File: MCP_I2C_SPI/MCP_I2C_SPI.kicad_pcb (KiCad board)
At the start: 2 copper layers, 136 x 95 mm, 46 parts, among them J1 GPA, J10 VCC, J11 GND, J12 I2C, J13 Interrupt0, J14 A2, J15 A1, J16 A0, J17 SDA, J18 SCK, J19 INTA, J2 GPB, J20 INTB, J21 V0, J22 Ext, J23 SPI, J24 InterruptS, J25 A2, J27 GPB, J28 GPA, J29 A1, J3 Data, J31 A0, J32 INTA, J33 INTB, J4 Control, J5 Zlacze_LCD, J6 VSS, J7 K, J8 VDD, J9 A, U1 MCP23017_SP, U2 MCP23017_SP

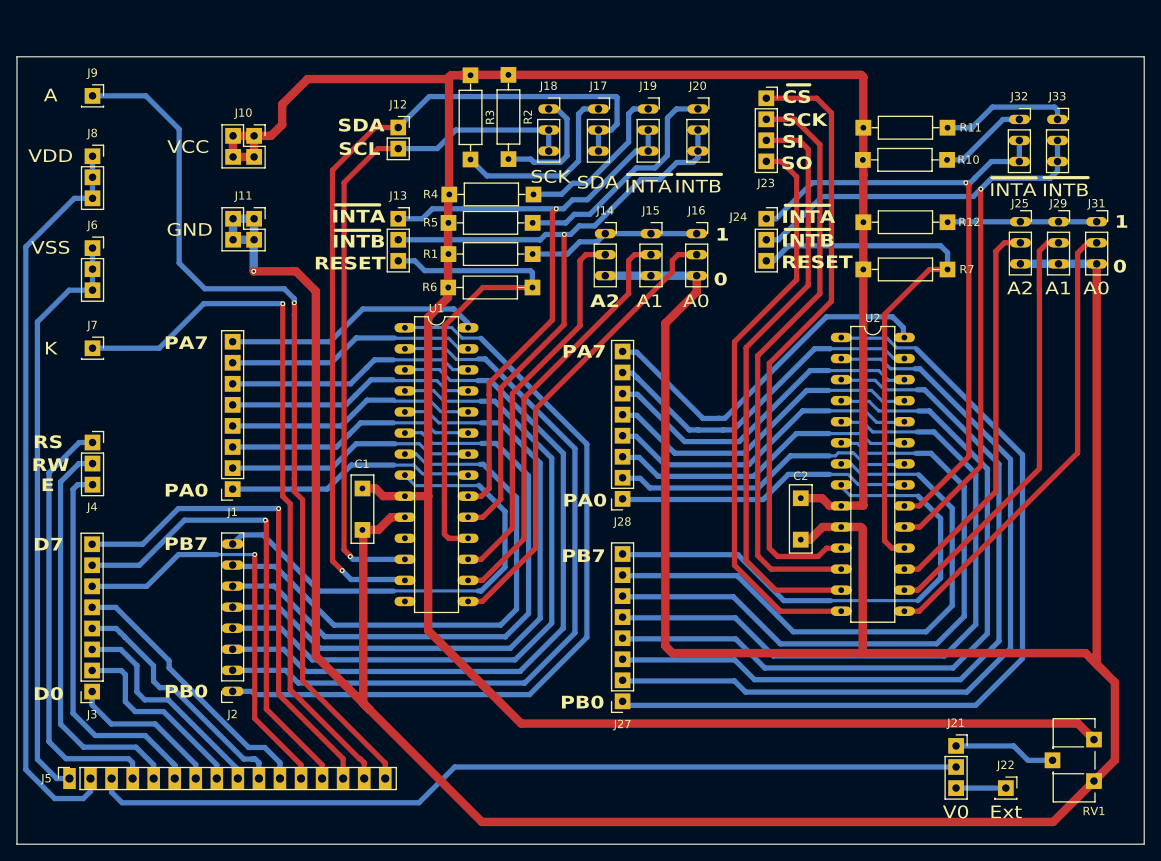
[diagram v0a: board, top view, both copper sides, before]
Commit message: Zmiana footprintu rezystorow - 6mm
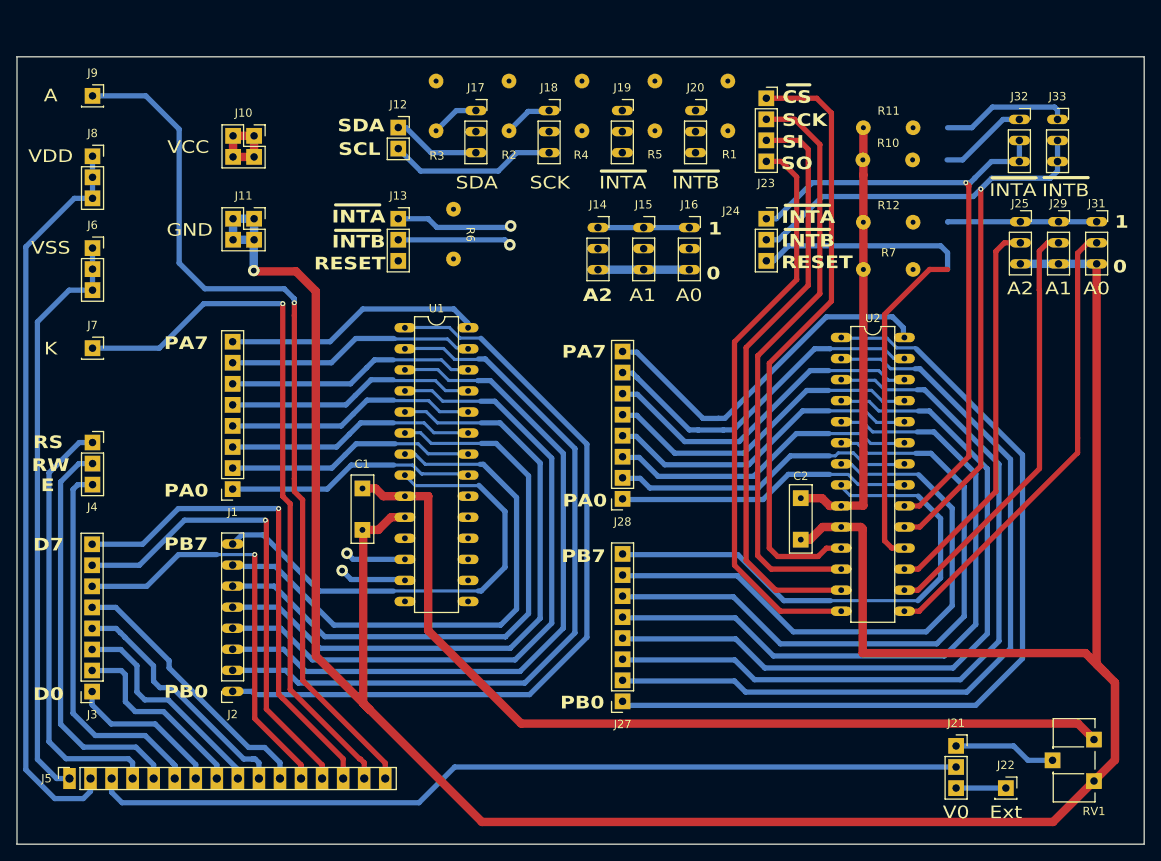
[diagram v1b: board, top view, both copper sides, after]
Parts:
- R1, R10, R11, R12, R2, R3, R4, R5, R6, R7: footprint Library:R_Axial_DIN0207_L6.3mm_D2.5mm_P10.16mm_Horizontal_square -> Library:Resistor_6mm
- moved R1 39.6 mm to (137.7, 28.2), turned to -90 degrees
- moved R5 30.2 mm to (128.9, 28.2), turned to -90 degrees
- moved R4 21.1 mm to (120.1, 28.2), turned to -90 degrees
- moved J17 14.8 mm to (107.3, 31.8)
- moved R6 9.47 mm to (104.6, 43.7), turned to -90 degrees
- moved R3 4.21 mm to (102.5, 28.2)
- moved J19 3.13 mm to (125.0, 31.8)
- moved J14 1.14 mm to (122.0, 45.9)
- moved J15 1.14 mm to (127.5, 45.9)
- moved J16 1.14 mm to (133.1, 45.9)
- moved R2 0.75 mm to (111.3, 28.2)
- moved J20 0.35 mm to (133.8, 31.8)
- moved J18 0.20 mm to (116.1, 31.8)
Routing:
- net +5V: track 311.0 -> 174.0 mm
- net SDA: track 103.2 -> 18.7 mm
- net GND: track 408.4 -> 338.0 mm
- net INTB0: track 83.6 -> 13.9 mm
- net INTA0: track 76.1 -> 14.2 mm
- net RESET0: track 60.0 -> 0.00 mm
- net Net-(J16-Pin_2): track 55.6 -> 0.00 mm
- net SCL: track 82.4 -> 27.5 mm
- net Net-(J15-Pin_2): track 50.6 -> 0.00 mm
- net Net-(J14-Pin_2): track 45.9 -> 0.00 mm
- net Net-(J20-Pin_1): track 28.3 -> 0.00 mm
- net Net-(J19-Pin_1): track 20.1 -> 0.00 mm
- net Net-(J17-Pin_1): track 22.9 -> 5.81 mm
- net Net-(J14-Pin_1): track 20.8 -> 11.0 mm
- net Net-(J18-Pin_1): track 14.7 -> 5.87 mm

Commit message: Update PCB MCP_I2C_SPI V3
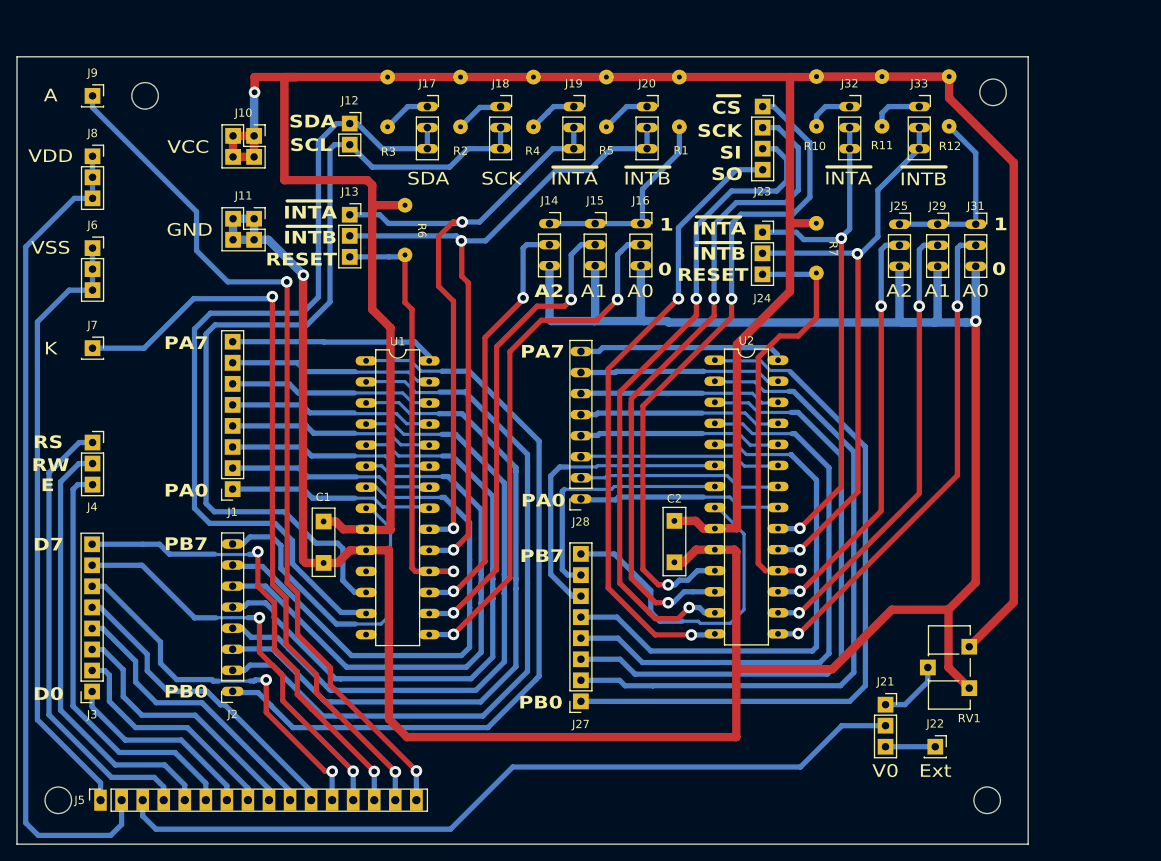
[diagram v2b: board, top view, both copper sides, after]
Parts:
- added REF**: MountingHole_3.2mm_M3, MountingHole:MountingHole_3.2mm_M3, F.Cu at (67.4, 30.0)
- added REF**: MountingHole_3.2mm_M3, MountingHole:MountingHole_3.2mm_M3, F.Cu at (56.9, 115.0)
- added REF**: MountingHole_3.2mm_M3, MountingHole:MountingHole_3.2mm_M3, F.Cu at (169.7, 29.6)
- added REF**: MountingHole_3.2mm_M3, MountingHole:MountingHole_3.2mm_M3, F.Cu at (169.0, 115.0)
- moved J32 20.5 mm to (152.4, 31.3)
- moved R12 20.4 mm to (164.4, 27.7), turned to -90 degrees
- moved RV1 18.8 mm to (166.8, 101.5)
- moved J33 16.7 mm to (160.8, 31.3)
- moved C2 15.5 mm to (131.3, 81.3)
- moved U2 15.5 mm to (136.1, 61.9)
- moved J29 14.6 mm to (163.0, 45.5)
- moved J25 14.6 mm to (158.4, 45.5)
- moved J31 14.6 mm to (167.6, 45.5)
- moved R10 11.5 mm to (148.4, 27.7), turned to -90 degrees
- moved J21 9.87 mm to (156.7, 103.5)
- moved J22 9.87 mm to (162.7, 108.6)
- moved R7 7.95 mm to (148.4, 45.4), turned to -90 degrees
- moved R11 6.57 mm to (156.3, 27.7), turned to -90 degrees
- moved C1 6.16 mm to (88.9, 81.4)
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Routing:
- net +5V: track 174.0 -> 322.8 mm, vias 0 -> 1
- net SDA: track 18.7 -> 102.3 mm, vias 1 -> 0
- net SCL: track 27.5 -> 106.8 mm, vias 1 -> 0
- net INTB0: track 13.9 -> 84.8 mm, vias 1 -> 2
- net Net-(J16-Pin_2): track 0.00 -> 64.2 mm, vias 0 -> 2
- net INTA0: track 14.2 -> 76.3 mm, vias 1 -> 2
- net Net-(J15-Pin_2): track 0.00 -> 57.6 mm, vias 0 -> 2
- net RESET0: track 0.00 -> 53.0 mm, vias 0 -> 1
- net Net-(J14-Pin_2): track 0.00 -> 51.3 mm, vias 0 -> 2
- net Net-(J27-Pin_7): track 71.2 -> 30.6 mm
- net Net-(J27-Pin_6): track 77.6 -> 38.0 mm
- net Net-(J27-Pin_8): track 62.6 -> 39.4 mm
- net Net-(J28-Pin_8): track 43.9 -> 24.9 mm
- net Net-(J27-Pin_5): track 83.8 -> 65.3 mm
- net Net-(J27-Pin_4): track 88.0 -> 70.0 mm
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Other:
- board size 136 x 95 mm -> 122 x 95 mm

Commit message: płytka MCP 17.06.2026
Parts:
- moved RV1 16.7 mm to (161.6, 85.6)
- moved J14 11.7 mm to (104.5, 45.4)
- moved J16 11.7 mm to (115.5, 45.4)
- moved J15 11.7 mm to (110.0, 45.4)
- moved J21 11.7 mm to (145.2, 105.6)
- moved J22 11.0 mm to (151.8, 107.9)
- moved J23 7.38 mm to (141.8, 38.7), turned to 180 degrees
- moved R6 6.65 mm to (92.1, 43.3)
- moved J10 6.58 mm to (74.0, 35.7)
- moved J11 6.58 mm to (74.0, 45.7)
- moved J25 6.23 mm to (152.3, 44.3)
- moved J29 6.23 mm to (156.9, 44.3)
- moved J31 6.23 mm to (161.5, 44.3)
- moved R1 6.10 mm to (125.8, 27.7)
- moved J20 5.88 mm to (122.1, 31.3)
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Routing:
- net INTB0: track 84.8 -> 129.0 mm
- net INTBS: track 71.3 -> 95.4 mm
- net Net-(J21-Pin_1): track 7.97 -> 30.4 mm
- net +5V: track 322.8 -> 304.9 mm
- net INTA0: track 76.3 -> 89.3 mm
- net Net-(J21-Pin_2): track 97.4 -> 85.0 mm
- net CS: track 81.2 -> 69.1 mm
- net GND: track 326.1 -> 337.8 mm
- net SO: track 75.3 -> 86.3 mm
- net Net-(J14-Pin_1): track 24.6 -> 30.4 mm
- net SCK: track 82.4 -> 76.8 mm
- net Net-(J16-Pin_2): track 64.2 -> 59.2 mm
- net Net-(J15-Pin_2): track 57.6 -> 53.2 mm
- net Net-(J5-Pin_15): track 91.2 -> 86.9 mm
- net RESETS: track 54.1 -> 50.4 mm
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
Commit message: kolejna wersja MCP
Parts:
- J10, J11: footprint Library:PinSocket_2x02_P2.54mm_Vertical_kwadrat -> Library:PinSocket_1x03_P2.54mm_Vertical
- moved RV1 32.4 mm to (140.6, 110.3), turned to 90 degrees
- moved R1 30.8 mm to (99.4, 43.6)
- moved J22 18.6 mm to (133.1, 108.1)
- moved J21 16.9 mm to (128.3, 105.5)
- moved J31 10.2 mm to (151.3, 44.3)
- moved J33 10.2 mm to (148.9, 31.2)
- moved R11 10.2 mm to (145.3, 27.7)
- moved J23 10.2 mm to (131.6, 38.7)
- moved J24 10.2 mm to (131.7, 46.5)
- moved J25 10.2 mm to (142.1, 44.3)
- moved J29 10.2 mm to (146.7, 44.3)
- moved J32 10.2 mm to (141.8, 31.3)
- moved R10 10.2 mm to (138.2, 27.7)
- moved R12 10.2 mm to (152.4, 27.7)
- moved R7 8.66 mm to (137.9, 45.3)
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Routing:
- net INTB0: track 129.0 -> 100.6 mm
- net GND: track 337.8 -> 312.7 mm
- net Net-(J27-Pin_8): track 39.4 -> 20.8 mm
- net Net-(J21-Pin_2): track 85.0 -> 68.1 mm
- net Net-(J21-Pin_1): track 30.4 -> 14.9 mm
- net +5V: track 304.9 -> 317.5 mm
- net Net-(J14-Pin_1): track 30.4 -> 19.4 mm
- net INTA0: track 89.3 -> 83.3 mm
- net Net-(J31-Pin_2): track 63.0 -> 57.1 mm
- net INTBS: track 95.4 -> 99.4 mm
- net CS: track 69.1 -> 65.4 mm
- net INTAS: track 63.5 -> 66.7 mm
- net SCL: track 103.6 -> 101.1 mm
- net RESETS: track 50.4 -> 52.9 mm
- net SDA: track 101.6 -> 99.2 mm
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
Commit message: MCP_I2C_SPI_V5
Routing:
- net INTA0: track 83.3 -> 86.3 mm
- net INTB0: track 100.6 -> 103.5 mm
- net SCK: track 74.6 -> 73.1 mm
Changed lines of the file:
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@@
 		)
 		(property "Value" "V0"
-			(at -3.6576 2.3114 0)
+			(at -3.8608 2.6538 0)
 			(layer "F.SilkS")
 			(effects
@@
 		)
 		(property "Value" "Ext"
-			(at -0.1778 3.0734 0)
+			(at -0.1214 3.373 0)
 			(layer "F.SilkS")
 			(effects
@@
 			)
 		)
-		(pad "1" thru_hole oval
+		(pad "1" thru_hole rect
 			(at 0 0)
-			(size 2.54 1.143)
-			(drill 0.508)
+			(size 1.905 1.905)
+			(drill 0.9)
 			(layers "*.Cu" "*.Mask")
 			(remove_unused_layers no)
@@
 			(pintype "passive")
 		)
-		(pad "2" thru_hole oval
+		(pad "2" thru_hole rect
 			(at 0 2.54)
-			(size 2.54 1.143)
-			(drill 0.508)
+			(size 1.905 1.905)
+			(drill 0.9)
 			(layers "*.Cu" "*.Mask")
 			(remove_unused_layers no)
@@
 			(pintype "passive")
 		)
-		(pad "3" thru_hole oval
+		(pad "3" thru_hole rect
 			(at 0 5.08)
-			(size 2.54 1.143)
-			(drill 0.508)
+			(size 1.905 1.905)
+			(drill 0.9)
 			(layers "*.Cu" "*.Mask")
 			(remove_unused_layers no)
@@
 			)
 		)
-		(pad "1" thru_hole oval
+		(pad "1" thru_hole rect
 			(at 0 0)
-			(size 2.54 1.143)
-			(drill 0.508)
+			(size 1.905 1.905)
+			(drill 0.9)
 			(layers "*.Cu" "*.Mask")
 			(remove_unused_layers no)
@@
 			(pintype "passive")
 		)
-		(pad "2" thru_hole oval
+		(pad "2" thru_hole rect
 			(at 0 2.54)
-			(size 2.54 1.143)
-			(drill 0.508)
+			(size 1.905 1.905)
+			(drill 0.9)
 			(layers "*.Cu" "*.Mask")
 			(remove_unused_layers no)
@@
 			(pintype "passive")
 		)
-		(pad "3" thru_hole oval
+		(pad "3" thru_hole rect
 			(at 0 5.08)
-			(size 2.54 1.143)
-			(drill 0.508)
+			(size 1.905 1.905)
+			(drill 0.9)
 			(layers "*.Cu" "*.Mask")
 			(remove_unused_layers no)
@@
 	)
 	(segment
-		(start 88.9289 95.932422)
-		(end 92.8878 99.891322)
+		(start 130.5306 90.5002)
+		(end 130.5306 86.8788)
 		(width 1.016)
 		(layer "F.Cu")
@@
 	)
 	(segment
-		(start 130.5306 90.5002)
-		(end 130.5306 86.8788)
+		(start 83.9617 56.547952)
+		(end 83.9617 80.244266)
 		(width 1.016)
 		(layer "F.Cu")
@@
 	)
 	(segment
-		(start 83.9617 56.547952)
-		(end 83.9617 80.244266)
+		(start 125.349 103.3018)
+		(end 125.349 98.8822)
 		(width 1.016)
 		(layer "F.Cu")
@@
 	)
 	(segment
-		(start 96.7926 105.2)
-		(end 96.8 105.2)
+		(start 80.981348 53.550348)
+		(end 80.981348 53.5676)
 		(width 1.016)
 		(layer "F.Cu")
@@
 	)
 	(segment
-		(start 125.349 103.3018)
-		(end 125.349 98.8822)
+		(start 92.72 99.723522)
+		(end 92.72 101.12)
 		(width 1.016)
 		(layer "F.Cu")
@@
 	)
 	(segment
-		(start 80.981348 53.550348)
-		(end 80.981348 53.5676)
+		(start 92.72 101.12)
+		(end 99 107.4)
 		(width 1.016)
 		(layer "F.Cu")
@@
 	)
 	(segment
-		(start 85.765499 82.048063)
-		(end 85.765501 85.365501)
+		(start 121.2508 107.4)
+		(end 125.349 103.3018)
 		(width 1.016)
 		(layer "F.Cu")
@@
 	)
 	(segment
-		(start 80.981348 53.5676)
-		(end 83.9617 56.547952)
+		(start 85.765499 82.048063)
+		(end 85.765501 85.365501)
 		(width 1.016)
 		(layer "F.Cu")
@@
 	)
 	(segment
-		(start 99 107.4)
-		(end 121.2508 107.4)
+		(start 80.981348 53.5676)
+		(end 83.9617 56.547952)
 		(width 1.016)
 		(layer "F.Cu")
@@
 	)
 	(segment
-		(start 92.8878 101.2952)
-		(end 96.7926 105.2)
+		(start 88.9289 95.932422)
+		(end 92.72 99.723522)
 		(width 1.016)
 		(layer "F.Cu")
@@
 	)
 	(segment
-		(start 96.8 105.2)
-		(end 99 107.4)
+		(start 99 107.4)
+		(end 121.2508 107.4)
 		(width 1.016)
 		(layer "F.Cu")
@@
 	)
 	(segment
-		(start 88.9289 86.385)
-		(end 88.9289 95.932422)
-		(width 1.016)
-		(layer "F.Cu")
-		(net 1)
-	)
-	(segment
 		(start 140.6144 98.8822)
 		(end 125.349 98.8822)
@@
 	)
 	(segment
-		(start 85.765501 85.365501)
-		(end 86.785 86.385)
+		(start 88.9289 86.385)
+		(end 88.9289 95.932422)
 		(width 1.016)
 		(layer "F.Cu")
@@
 	)
 	(segment
-		(start 92.8878 99.891322)
-		(end 92.8878 101.2952)
+		(start 85.765501 85.365501)
+		(end 86.785 86.385)
 		(width 1.016)
 		(layer "F.Cu")
@@
 	)
 	(segment
-		(start 121.2508 107.4)
-		(end 125.349 103.3018)
-		(width 1.016)
-		(layer "F.Cu")
-		(net 1)
-	)
-	(segment
 		(start 125.349 95.6818)
 		(end 130.5306 90.5002)
@@
 	)
 	(segment
-		(start 81.9614 89.175)
-		(end 84.112 91.3256)
-		(width 0.381)
-		(layer "B.Cu")
-		(net 14)
-	)
-	(segment
 		(start 107.938982 90.070622)
 		(end 107.93898 91.228744)
@@
 	)
 	(segment
+		(start 81.9614 89.175)
+		(end 84.112 91.3256)
+		(width 0.381)
+		(layer "B.Cu")
+		(net 14)
+	)
+	(segment
 		(start 95.93178 74.6593)
 		(end 95.1016 74.6593)
@@
 	)
 	(segment
-		(start 84.112 92.85734)
-		(end 90.20866 98.954)
-		(width 0.381)
-		(layer "B.Cu")
-		(net 14)
-	)
-	(segment
 		(start 107.938992 88.912478)
 		(end 107.938988 88.912482)
@@
 	)
 	(segment
-		(start 90.20866 98.954)
-		(end 91.726929 98.954)
+		(start 84.112 92.85734)
+		(end 90.20866 98.954)
 		(width 0.381)
 		(layer "B.Cu")
@@
 	)
 	(segment
-		(start 81.94793 89.23773)
-		(end 81.94793 89.175)
+		(start 77.9621 89.1659)
+		(end 77.953 89.175)
 		(width 0.381)
 		(layer "B.Cu")
@@
 	)
 	(segment
-		(start 77.9621 89.1659)
-		(end 77.953 89.175)
+		(start 90.20866 98.954)
+		(end 91.726929 98.954)
 		(width 0.381)
 		(layer "B.Cu")
@@
 	)
 	(segment
-		(start 81.94793 89.175)
-		(end 81.9614 89.175)
-		(width 0.381)
-		(layer "B.Cu")
-		(net 14)
-	)
-	(segment
 		(start 107.939 91.228786)
 		(end 107.939 97.15272)
@@
 	)
 	(segment
+		(start 104.54 84.86)
+		(end 104.6 84.8)
+		(width 0.635)
+		(layer "F.Cu")
+		(net 49)
+	)
+	(segment
+		(start 101.6739 84.86)
+		(end 104.54 84.86)
+		(width 0.635)
+		(layer "F.Cu")
+		(net 49)
+	)
+	(segment
 		(start 98.3439 84.86)
 		(end 101.6739 84.86)
@@
 	)
 	(segment
+		(start 101.6739 82.32)
+		(end 104.48 82.32)
+		(width 0.635)
+		(layer "F.Cu")
+		(net 50)
+	)
+	(segment
 		(start 94.9198 56.007)
 		(end 97.023 56.007)
@@
 	)
 	(segment
+		(start 104.48 82.32)
+		(end 104.6 82.2)
+		(width 0.635)
+		(layer "F.Cu")
+		(net 50)
+	)
+	(segment
 		(start 100.0238 82.32)
 		(end 101.6739 82.32)
@@
 		(width 0.635)
 		(layer "F.Cu")
-		(net 55)
-	)
-	(segment
-		(start 126.05674 68.4)
-		(end 126.05674 66.9)
-		(width 0.635)
-		(layer "F.Cu")

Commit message: MCP_I2C_SPI_PCB_V6
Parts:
- removed R1, R4, R5, R6: 10k, Library:Resistor_6mm
- removed R2, R3: 4k7, Library:Resistor_6mm
- added J65: SIL6, Connector_PinSocket_2.54mm:PinSocket_1x06_P2.54mm_Vertical, F.Cu at (91.8, 29.0)
- added R16: 10k, Library:Resistor_6mm, F.Cu at (91.0, 55.3)
- moved REF** 22.5 mm to (146.5, 115.5)
- moved REF** 15.8 mm to (154.0, 28.0)
- moved J20 15.7 mm to (103.4, 38.4), turned to -90 degrees
- moved J16 14.1 mm to (103.6, 52.9), turned to -90 degrees
- moved J17 9.10 mm to (103.4, 26.1), turned to -90 degrees
- moved J32 8.98 mm to (132.9, 30.2)
- moved R10 8.98 mm to (129.3, 26.6)
- moved R12 8.98 mm to (143.5, 26.6)
- moved J23 8.98 mm to (122.7, 37.6)
- moved J24 8.98 mm to (122.8, 45.4)
- moved J25 8.98 mm to (133.2, 43.3)
- moved J29 8.98 mm to (137.8, 43.3)
- moved J31 8.98 mm to (142.4, 43.3)
- moved J33 8.98 mm to (139.9, 30.2)
- moved R11 8.98 mm to (136.4, 26.6)
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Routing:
- net INTB0: track 103.5 -> 83.7 mm
- net Net-(J14-Pin_2): track 50.0 -> 63.8 mm
- net INTBS: track 99.4 -> 108.8 mm
- net Net-(J17-Pin_1): track 5.43 -> 14.6 mm
- net RESET0: track 56.3 -> 65.3 mm
- net Net-(J16-Pin_2): track 59.7 -> 50.9 mm
- net Net-(J20-Pin_1): track 5.52 -> 13.9 mm
- net INTAS: track 66.7 -> 75.0 mm
- net Net-(J18-Pin_1): track 5.53 -> 13.8 mm
- net SI: track 79.8 -> 88.0 mm
- net Net-(J19-Pin_1): track 5.29 -> 13.4 mm
- net +5V: track 317.5 -> 309.5 mm
- net Net-(J14-Pin_1): track 19.4 -> 27.4 mm
- net Net-(J25-Pin_2): track 51.3 -> 59.3 mm
- net SO: track 86.3 -> 94.0 mm
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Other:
- board size 122 x 95 mm -> 107 x 99 mm

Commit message: Płytka MCP_I2C_SPI_V7
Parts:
- removed R10, R11, R12, R16, R7: 10k, Library:Resistor_6mm
- added J66: SIL5, Connector_PinSocket_2.54mm:PinSocket_1x05_P2.54mm_Vertical, F.Cu at (128.8, 29.9)
- J65: value SIL6 -> SIL7; footprint Connector_PinSocket_2.54mm:PinSocket_1x06_P2.54mm_Vertical -> Connector_PinSocket_2.54mm:PinSocket_1x07_P2.54mm_Vertical
- moved REF** 11.6 mm to (57.0, 24.8)
- moved REF** 8.75 mm to (145.9, 24.7)
- moved J25 6.49 mm to (139.2, 40.9), turned to -90 degrees
- moved RV1 6.29 mm to (144.0, 105.0), turned to -90 degrees
- moved J32 6.22 mm to (139.1, 30.0), turned to -90 degrees
- moved J31 6.09 mm to (139.3, 48.5), turned to -90 degrees
- moved J33 4.69 mm to (139.0, 34.8), turned to -90 degrees
- moved U2 2.13 mm to (134.0, 61.9)
- moved J29 2.08 mm to (139.3, 44.7), turned to -90 degrees
- moved J24 1.63 mm to (122.7, 43.8)
- moved U1 1.05 mm to (93.0, 62.0)
- moved J65 0.07 mm to (91.8, 29.0)
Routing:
- net INTBS: track 108.8 -> 75.3 mm
- net Net-(J27-Pin_5): track 65.3 -> 41.2 mm
- net Net-(J25-Pin_2): track 59.3 -> 70.8 mm
- net GND: track 310.9 -> 302.5 mm
- net Net-(J2-Pin_2): track 91.8 -> 84.2 mm
- net Net-(J27-Pin_4): track 70.0 -> 62.7 mm
- net Net-(J27-Pin_3): track 75.6 -> 68.2 mm
- net Net-(J33-Pin_1): track 5.30 -> 12.4 mm
- net Net-(J2-Pin_7): track 64.1 -> 57.1 mm
- net Net-(J27-Pin_1): track 86.7 -> 79.9 mm
- net Net-(J27-Pin_2): track 80.9 -> 74.0 mm
- net Net-(J32-Pin_1): track 5.59 -> 12.0 mm
- net Net-(J2-Pin_1): track 94.7 -> 88.9 mm
- net Net-(J2-Pin_3): track 85.8 -> 80.2 mm
- net RESETS: track 59.2 -> 64.8 mm, vias 1 -> 2
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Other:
- board size 107 x 99 mm -> 99.7 x 99.8 mm
- board text added: "I2C"
- board text added: "SPI"

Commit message: MCP_I2C_SPI PCB V8
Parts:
- moved RV1 5.11 mm to (144.3, 110.1), turned to 180 degrees
- moved REF** 2.33 mm to (144.4, 116.5)
- moved REF** 1.60 mm to (144.3, 24.6)
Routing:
- net GND: track 302.5 -> 280.5 mm, vias 2 -> 5
- net SDA: track 104.1 -> 121.9 mm
- net Net-(J29-Pin_2): track 59.2 -> 73.0 mm
- net +5V: track 308.3 -> 318.0 mm, vias 2 -> 4
- net Net-(J15-Pin_2): track 51.6 -> 59.8 mm
- net Net-(J5-Pin_16): track 108.6 -> 114.2 mm
- net Net-(J27-Pin_4): track 62.7 -> 58.4 mm
- net SCL: track 95.2 -> 99.1 mm
- net Net-(J21-Pin_1): track 15.0 -> 11.9 mm
- net SO: track 89.6 -> 92.5 mm
- net SI: track 83.3 -> 86.1 mm
- net Net-(J27-Pin_1): track 79.9 -> 77.5 mm
- net Net-(J27-Pin_3): track 68.2 -> 65.8 mm
- net Net-(J27-Pin_2): track 74.0 -> 71.7 mm
- net SCK: track 77.9 -> 79.9 mm
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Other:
- board size 99.7 x 99.8 mm -> 97.7 x 99.8 mm
